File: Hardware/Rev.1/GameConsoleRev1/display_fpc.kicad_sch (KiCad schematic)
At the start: 15 parts, among them J10 Conn_01x40, J11 Conn_01x08_Pin, J12 Conn_01x08_Pin, Q3 NTR1P02T1G

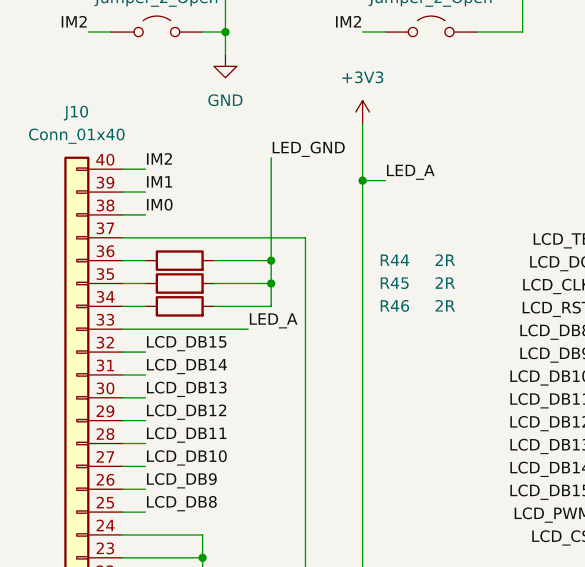
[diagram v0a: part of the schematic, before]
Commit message: Added CPP Build
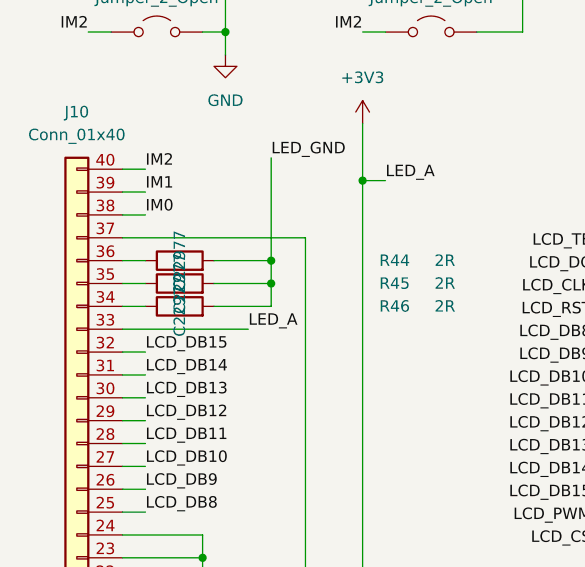
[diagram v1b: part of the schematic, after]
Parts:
- R44, R45, R46: LCSC (none) -> C22977
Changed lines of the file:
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@@
+			)
+		)
+		(property "DK" ""
+			(at 60.96 63.5 0)
+			(effects
+				(font
+					(size 1.27 1.27)
+				)
+			)
+		)
+		(property "LCSC" "C22977"
+			(at 60.96 63.5 0)
+			(effects
+				(font
+					(size 1.27 1.27)
+				)
 			)
 		)
@@
 			)
 		)
+		(property "DK" ""
+			(at 60.96 66.04 0)
+			(effects
+				(font
+					(size 1.27 1.27)
+				)
+			)
+		)
+		(property "LCSC" "C22977"
+			(at 60.96 66.04 0)
+			(effects
+				(font
+					(size 1.27 1.27)
+				)
+			)
+		)
 		(pin "1"
 		)
@@
 				)
 				(hide yes)
+			)
+		)
+		(property "DK" ""
+			(at 60.96 60.96 0)
+			(effects
+				(font
+					(size 1.27 1.27)
+				)
+			)
+		)
+		(property "LCSC" "C22977"
+			(at 60.96 60.96 0)
+			(effects
+				(font
+					(size 1.27 1.27)
+				)
 			)
 		)
@@
 			)
 		)
+		(property "DK" ""
+			(at 165.1 78.74 0)
+			(effects
+				(font
+					(size 1.27 1.27)
+				)
+			)
+		)
 		(pin "7"
 		)
@@
 			)
 		)
+		(property "DK" ""
+			(at 49.53 101.6 0)
+			(effects
+				(font
+					(size 1.27 1.27)
+				)
+			)
+		)
 		(pin "1"
 		)
@@
 			)
 		)
+		(property "DK" ""
+			(at 88.9 27.94 0)
+			(effects
+				(font
+					(size 1.27 1.27)
+				)
+			)
+		)
 		(pin "1"
 		)
@@
 			)
 		)
+		(property "DK" ""
+			(at 88.9 20.32 0)
+			(effects
+				(font
+					(size 1.27 1.27)
+				)
+			)
+		)
 		(pin "1"
 		)
@@
 		)
 		(property "Adjusted Value for stock" ""
+			(at 196.85 44.45 0)
+			(effects
+				(font
+					(size 1.27 1.27)
+				)
+			)
+		)
+		(property "DK" ""
 			(at 196.85 44.45 0)
 			(effects
@@
 			)
 		)
+		(property "DK" ""
+			(at 88.9 35.56 0)
+			(effects
+				(font
+					(size 1.27 1.27)
+				)
+			)
+		)
 		(pin "1"
 		)
@@
 			)
 		)
+		(property "DK" ""
+			(at 130.81 35.56 0)
+			(effects
+				(font
+					(size 1.27 1.27)
+				)
+			)
+		)
 		(pin "3"
 		)
@@
 			)
 		)
+		(property "DK" ""
+			(at 58.42 20.32 0)
+			(effects
+				(font
+					(size 1.27 1.27)
+				)
+			)
+		)
 		(pin "1"
 		)
@@
 			)
 		)
+		(property "DK" ""
+			(at 208.28 44.45 0)
+			(effects
+				(font
+					(size 1.27 1.27)
+				)
+			)
+		)
 		(pin "1"
 		)
@@
 			)
 		)
+		(property "DK" ""
+			(at 58.42 27.94 0)
+			(effects
+				(font
+					(size 1.27 1.27)
+				)
+			)
+		)
 		(pin "1"
 		)
@@
 			)
 		)
+		(property "DK" ""
+			(at 140.97 78.74 0)
+			(effects
+				(font
+					(size 1.27 1.27)
+				)
+			)
+		)
 		(pin "7"
 		)
@@
 			)
 		)
+		(property "DK" ""
+			(at 58.42 35.56 0)
+			(effects
+				(font
+					(size 1.27 1.27)
+				)
+			)
+		)
